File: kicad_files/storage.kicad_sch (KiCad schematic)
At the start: 12 parts, among them J7 Micro_SD_Card_Det2, U10 W25Q128JVS

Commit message: reset symbol annotations
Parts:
- renumbered C58 to C50, C59 to C51, C60 to C52, R18 to R15, R19 to R16, R20 to R17, R21 to R18, R22 to R19, R23 to R20, R24 to R21
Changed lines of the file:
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@@
 		(dnp no)
 		(fields_autoplaced yes)
-		(property "Reference" "R22"
+		(property "Reference" "R19"
 			(at 140.97 66.0399 0)
 			(show_name no)
@@
 			(project "versorlite"
 				(path "/1a230af0-0a74-48f7-8607-b087121dda49/7fbeed45-b545-4efe-b68f-fc15ad17addf"
-					(reference "R22")
+					(reference "R19")
 					(unit 1)
 				)
@@
 		(dnp no)
 		(fields_autoplaced yes)
-		(property "Reference" "C58"
+		(property "Reference" "C50"
 			(at 30.48 52.0762 0)
 			(show_name no)
@@
 			(project "versorlite"
 				(path "/1a230af0-0a74-48f7-8607-b087121dda49/7fbeed45-b545-4efe-b68f-fc15ad17addf"
-					(reference "C58")
+					(reference "C50")
 					(unit 1)
 				)
@@
 		(dnp no)
 		(fields_autoplaced yes)
-		(property "Reference" "C60"
+		(property "Reference" "C52"
 			(at 198.12 85.0899 0)
 			(show_name no)
@@
 			(project "versorlite"
 				(path "/1a230af0-0a74-48f7-8607-b087121dda49/7fbeed45-b545-4efe-b68f-fc15ad17addf"
-					(reference "C60")
+					(reference "C52")
 					(unit 1)
 				)
@@
 		(dnp no)
 		(fields_autoplaced yes)
-		(property "Reference" "R18"
+		(property "Reference" "R15"
 			(at 71.12 24.1299 0)
 			(show_name no)
@@
 			(project "versorlite"
 				(path "/1a230af0-0a74-48f7-8607-b087121dda49/7fbeed45-b545-4efe-b68f-fc15ad17addf"
-					(reference "R18")
+					(reference "R15")
 					(unit 1)
 				)
@@
 		(dnp no)
 		(fields_autoplaced yes)
-		(property "Reference" "C59"
+		(property "Reference" "C51"
 			(at 38.1 52.0762 0)
 			(show_name no)
@@
 			(project "versorlite"
 				(path "/1a230af0-0a74-48f7-8607-b087121dda49/7fbeed45-b545-4efe-b68f-fc15ad17addf"
-					(reference "C59")
+					(reference "C51")
 					(unit 1)
 				)
@@
 		(dnp no)
 		(fields_autoplaced yes)
-		(property "Reference" "R20"
+		(property "Reference" "R17"
 			(at 77.47 24.1299 0)
 			(show_name no)
@@
 			(project "versorlite"
 				(path "/1a230af0-0a74-48f7-8607-b087121dda49/7fbeed45-b545-4efe-b68f-fc15ad17addf"
-					(reference "R20")
+					(reference "R17")
 					(unit 1)
 				)
@@
 		(dnp no)
 		(fields_autoplaced yes)
-		(property "Reference" "R21"
+		(property "Reference" "R18"
 			(at 90.17 24.1299 0)
 			(show_name no)
@@
 			(project "versorlite"
 				(path "/1a230af0-0a74-48f7-8607-b087121dda49/7fbeed45-b545-4efe-b68f-fc15ad17addf"
-					(reference "R21")
+					(reference "R18")
 					(unit 1)
 				)
@@
 		(dnp no)
 		(fields_autoplaced yes)
-		(property "Reference" "R24"
+		(property "Reference" "R21"
 			(at 149.86 66.0399 0)
 			(show_name no)
@@
 			(project "versorlite"
 				(path "/1a230af0-0a74-48f7-8607-b087121dda49/7fbeed45-b545-4efe-b68f-fc15ad17addf"
-					(reference "R24")
+					(reference "R21")
 					(unit 1)
 				)
@@
 		(dnp no)
 		(fields_autoplaced yes)
-		(property "Reference" "R19"
+		(property "Reference" "R16"
 			(at 74.93 34.2899 0)
 			(show_name no)
@@
 			(project "versorlite"
 				(path "/1a230af0-0a74-48f7-8607-b087121dda49/7fbeed45-b545-4efe-b68f-fc15ad17addf"
-					(reference "R19")
+					(reference "R16")
 					(unit 1)
 				)
@@
 		(dnp no)
 		(fields_autoplaced yes)
-		(property "Reference" "R23"
+		(property "Reference" "R20"
 			(at 139.7 85.09 90)
 			(show_name no)
@@
 			(project "versorlite"
 				(path "/1a230af0-0a74-48f7-8607-b087121dda49/7fbeed45-b545-4efe-b68f-fc15ad17addf"
-					(reference "R23")
-					(unit 1)
-				)
+					(reference "R20")
+					(unit 1)
+				)

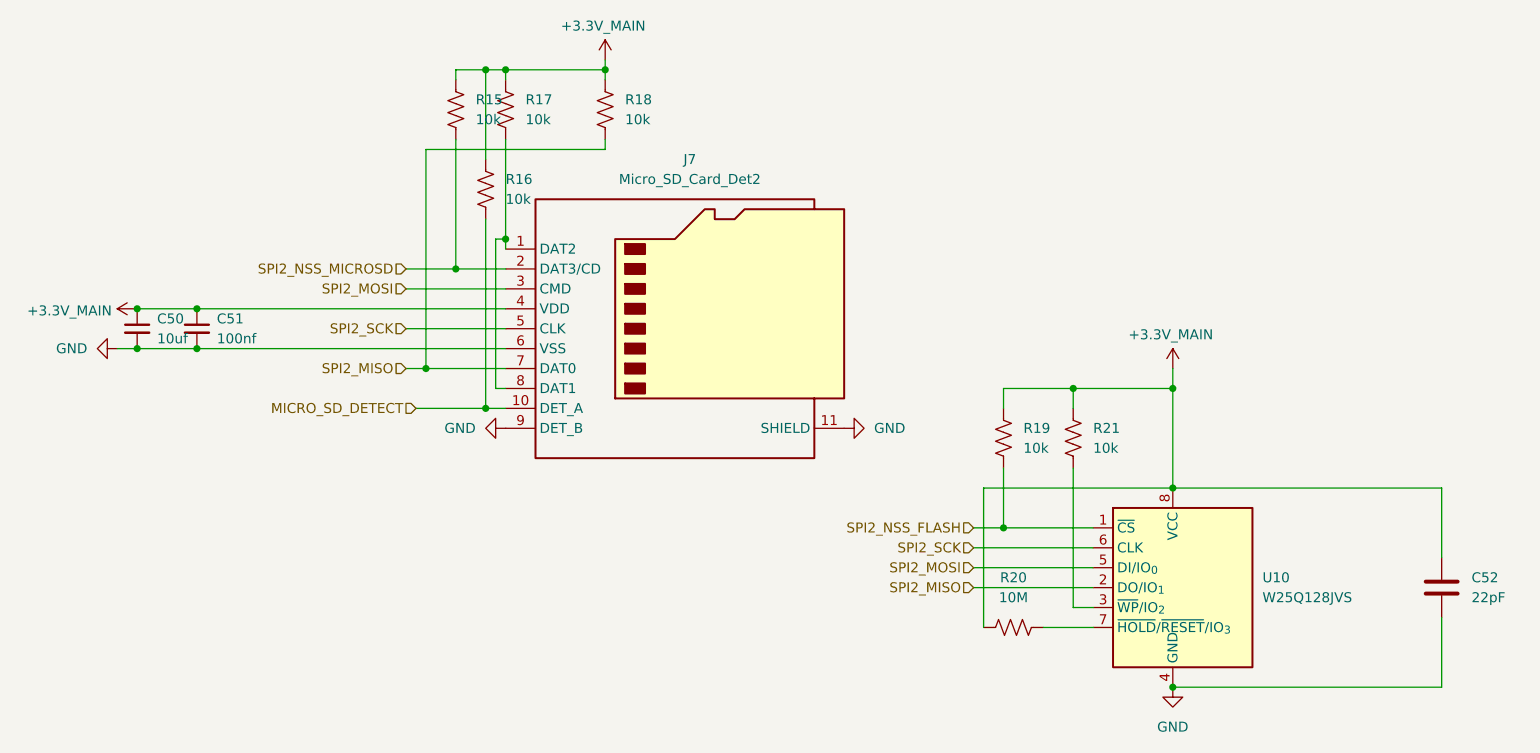
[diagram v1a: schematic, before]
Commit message: add dedicated power switching
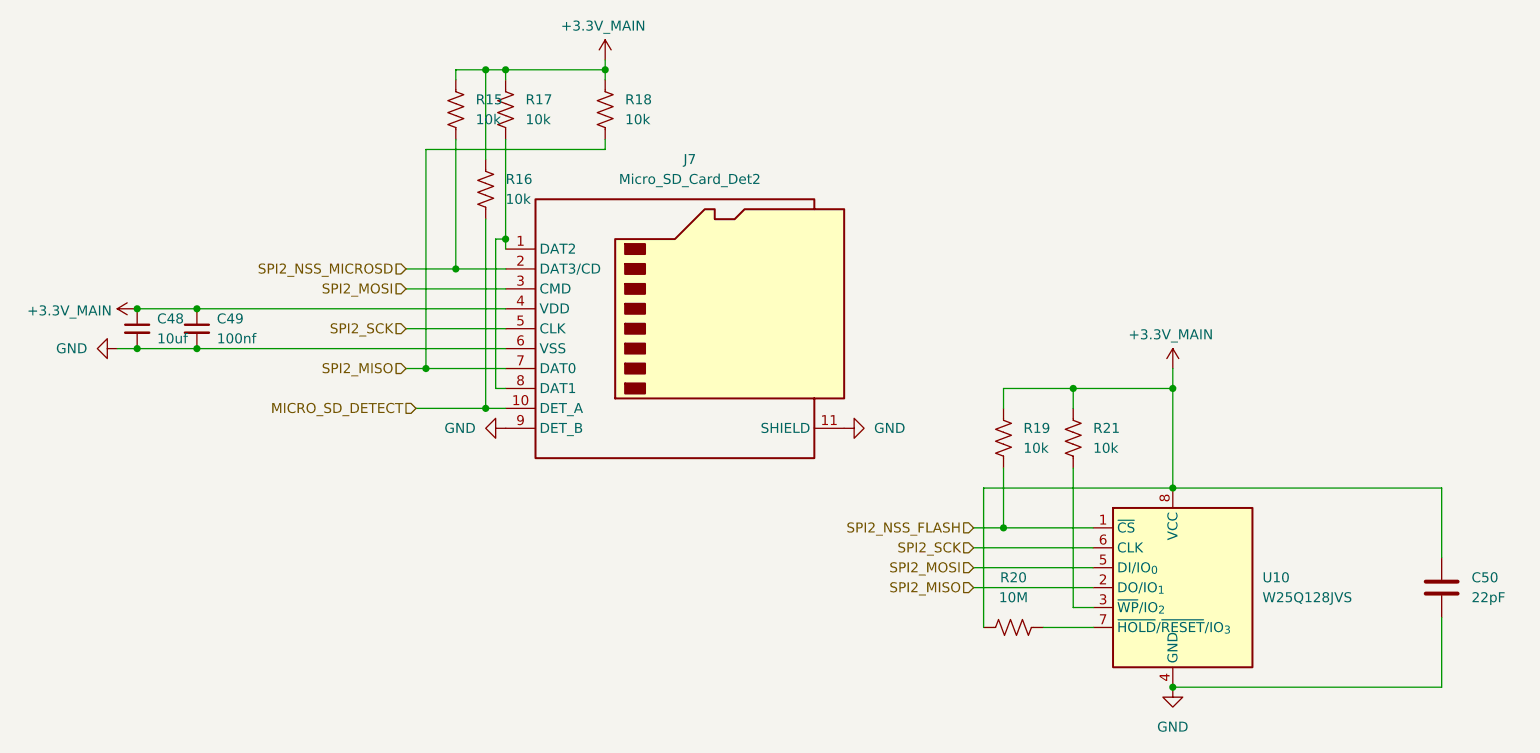
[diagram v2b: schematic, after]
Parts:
- renumbered C50 to C48, C51 to C49, C52 to C50
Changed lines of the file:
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@@
 		(in_pos_files yes)
 		(dnp no)
-		(property "Reference" "#PWR078"
+		(property "Reference" "#PWR073"
 			(at 31.75 50.8 0)
 			(hide yes)
@@
 			(project "versorlite"
 				(path "/1a230af0-0a74-48f7-8607-b087121dda49/7fbeed45-b545-4efe-b68f-fc15ad17addf"
-					(reference "#PWR078")
+					(reference "#PWR073")
 					(unit 1)
 				)
@@
 		(dnp no)
 		(fields_autoplaced yes)
-		(property "Reference" "#PWR079"
+		(property "Reference" "#PWR074"
 			(at 68.58 66.04 0)
 			(hide yes)
@@
 			(project "versorlite"
 				(path "/1a230af0-0a74-48f7-8607-b087121dda49/7fbeed45-b545-4efe-b68f-fc15ad17addf"
-					(reference "#PWR079")
+					(reference "#PWR074")
 					(unit 1)
 				)
@@
 		(dnp no)
 		(fields_autoplaced yes)
-		(property "Reference" "C50"
+		(property "Reference" "C48"
 			(at 30.48 52.0762 0)
 			(show_name no)
@@
 			(project "versorlite"
 				(path "/1a230af0-0a74-48f7-8607-b087121dda49/7fbeed45-b545-4efe-b68f-fc15ad17addf"
-					(reference "C50")
+					(reference "C48")
 					(unit 1)
 				)
@@
 		(in_pos_files yes)
 		(dnp no)
-		(property "Reference" "#PWR082"
+		(property "Reference" "#PWR077"
 			(at 160.02 62.23 0)
 			(hide yes)
@@
 			(project "versorlite"
 				(path "/1a230af0-0a74-48f7-8607-b087121dda49/7fbeed45-b545-4efe-b68f-fc15ad17addf"
-					(reference "#PWR082")
+					(reference "#PWR077")
 					(unit 1)
 				)
@@
 		(dnp no)
 		(fields_autoplaced yes)
-		(property "Reference" "C52"
+		(property "Reference" "C50"
 			(at 198.12 85.0899 0)
 			(show_name no)
@@
 			(project "versorlite"
 				(path "/1a230af0-0a74-48f7-8607-b087121dda49/7fbeed45-b545-4efe-b68f-fc15ad17addf"
-					(reference "C52")
+					(reference "C50")
 					(unit 1)
 				)
@@
 		(in_pos_files yes)
 		(dnp no)
-		(property "Reference" "#PWR080"
+		(property "Reference" "#PWR075"
 			(at 87.63 22.86 0)
 			(hide yes)
@@
 			(project "versorlite"
 				(path "/1a230af0-0a74-48f7-8607-b087121dda49/7fbeed45-b545-4efe-b68f-fc15ad17addf"
-					(reference "#PWR080")
+					(reference "#PWR075")
 					(unit 1)
 				)
@@
 		(dnp no)
 		(fields_autoplaced yes)
-		(property "Reference" "#PWR077"
+		(property "Reference" "#PWR072"
 			(at 19.05 55.88 0)
 			(hide yes)
@@
 			(project "versorlite"
 				(path "/1a230af0-0a74-48f7-8607-b087121dda49/7fbeed45-b545-4efe-b68f-fc15ad17addf"
-					(reference "#PWR077")
+					(reference "#PWR072")
 					(unit 1)
 				)
@@
 		(dnp no)
 		(fields_autoplaced yes)
-		(property "Reference" "C51"
+		(property "Reference" "C49"
 			(at 38.1 52.0762 0)
 			(show_name no)
@@
 			(project "versorlite"
 				(path "/1a230af0-0a74-48f7-8607-b087121dda49/7fbeed45-b545-4efe-b68f-fc15ad17addf"
-					(reference "C51")
+					(reference "C49")
 					(unit 1)
 				)
@@
 		(dnp no)
 		(fields_autoplaced yes)
-		(property "Reference" "#PWR083"
+		(property "Reference" "#PWR078"
 			(at 160.02 105.41 0)
 			(hide yes)
@@
 			(project "versorlite"
 				(path "/1a230af0-0a74-48f7-8607-b087121dda49/7fbeed45-b545-4efe-b68f-fc15ad17addf"
-					(reference "#PWR083")
+					(reference "#PWR078")
 					(unit 1)
 				)
@@
 		(dnp no)
 		(fields_autoplaced yes)
-		(property "Reference" "#PWR081"
+		(property "Reference" "#PWR076"
 			(at 124.46 66.04 0)
 			(hide yes)
@@
 			(project "versorlite"
 				(path "/1a230af0-0a74-48f7-8607-b087121dda49/7fbeed45-b545-4efe-b68f-fc15ad17addf"
-					(reference "#PWR081")
-					(unit 1)
-				)
+					(reference "#PWR076")
+					(unit 1)
+				)

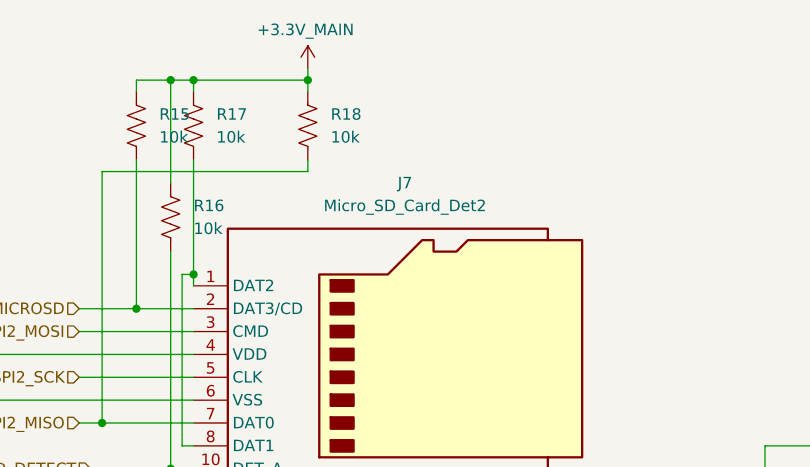
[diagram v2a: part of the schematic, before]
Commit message: size polyfuse, final drc stuff
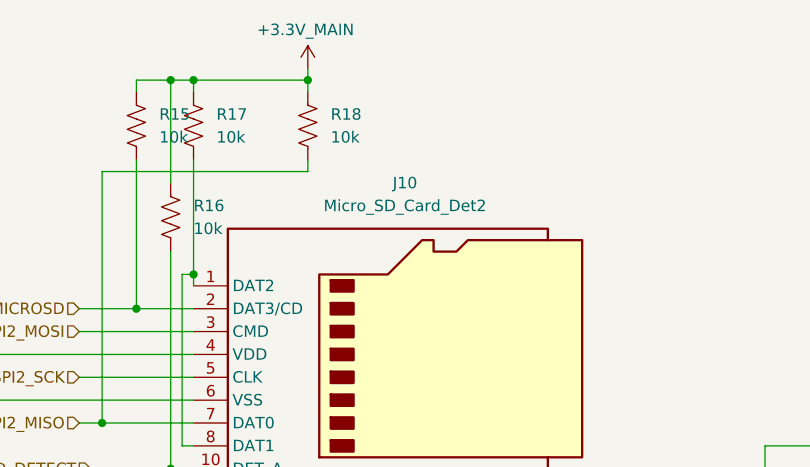
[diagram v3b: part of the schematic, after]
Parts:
- renumbered J7 to J10
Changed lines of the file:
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@@
 		(dnp no)
 		(fields_autoplaced yes)
-		(property "Reference" "J7"
+		(property "Reference" "J10"
 			(at 98.425 31.75 0)
 			(show_name no)
@@
 			(project "versorlite"
 				(path "/1a230af0-0a74-48f7-8607-b087121dda49/7fbeed45-b545-4efe-b68f-fc15ad17addf"
-					(reference "J7")
+					(reference "J10")
 					(unit 1)
 				)

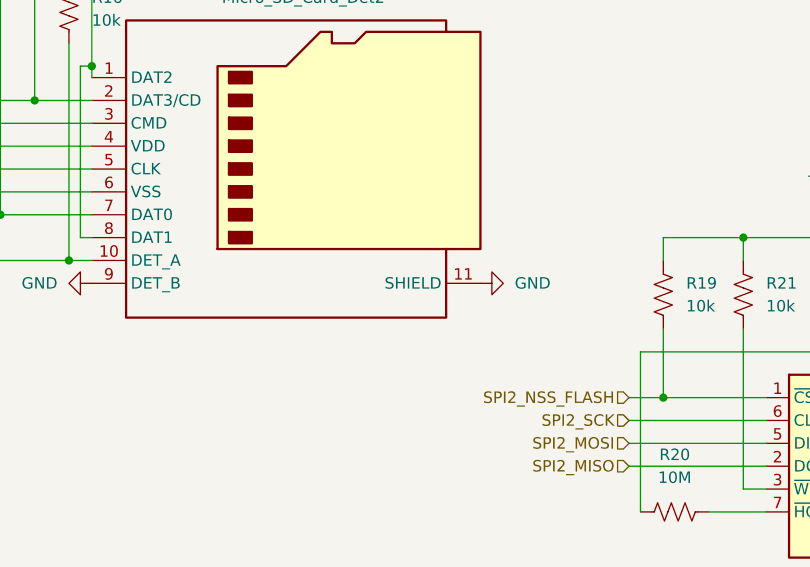
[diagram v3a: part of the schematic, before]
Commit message: fix thermal vias
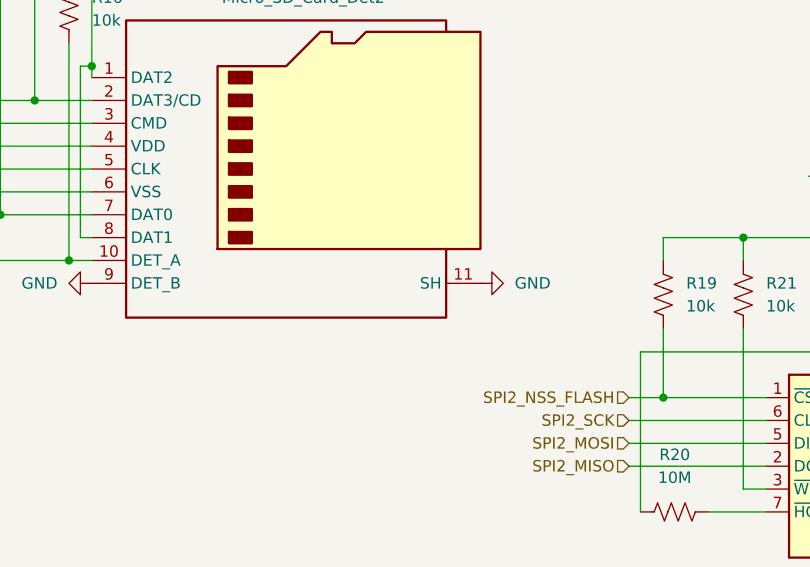
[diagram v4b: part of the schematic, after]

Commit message: fix thermal spoking
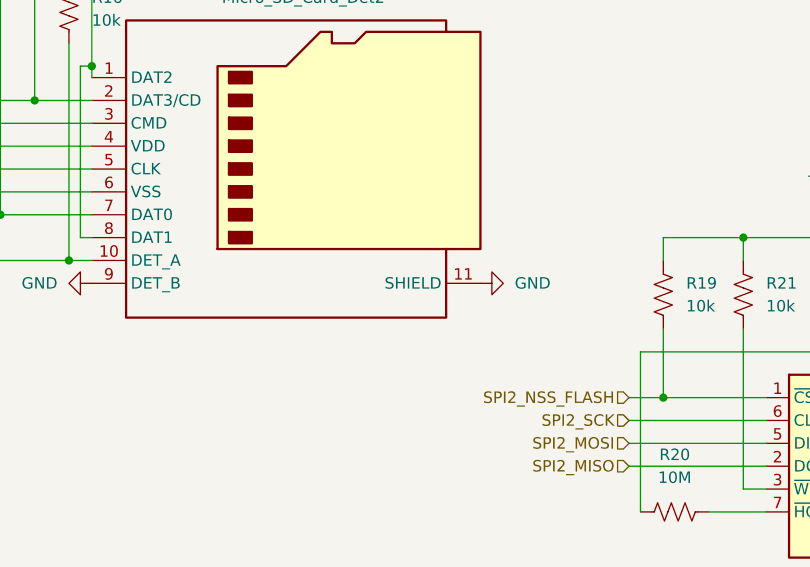
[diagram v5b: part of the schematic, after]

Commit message: fix ign
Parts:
- C50: value 22pF -> 100nF
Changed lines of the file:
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@@
 			)
 		)
-		(property "Value" "22pF"
+		(property "Value" "100nF"
 			(at 198.12 87.6299 0)
 			(show_name no)
